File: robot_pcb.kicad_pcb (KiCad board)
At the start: 4 copper layers, 140 x 180 mm, 196 parts, among them J1 Raspberry_Pi_2_3, J10 Servo_TrayRelease, J14 Motor FR, J17 Programmer, J18 USB_C_Receptacle_PowerOnly_6P, J2 Power_Bypass, J23 Motor BR, J25 ConductClaw, J26 Motor BL, J27 TOF_Front, J28 OLED_Display, J29 Motor FL, J3 Lipo, J4 TOF_Right, J5 TOF_Back, J6 TOF_Claw, J7 UltraS_Side, J8 Servo_Grab, J9 Servo_Lift, Q2 Q_NMOS_GDS, SW1 SW_SPDT, SW2 SW_Push, U1 STM32F407VGTx, U10 DMG2305UX-7, U11 DMG2305UX-7, U2 BQ76920PW, U3 AP64501SP-13, U4 MAX25240AFFD/VY+, U5 DMG2305UX-7, U6 AP64501SP-13, U7 AP64501SP-13, U9 BNO086, Y1 25MHz, Y2 32.768kHz

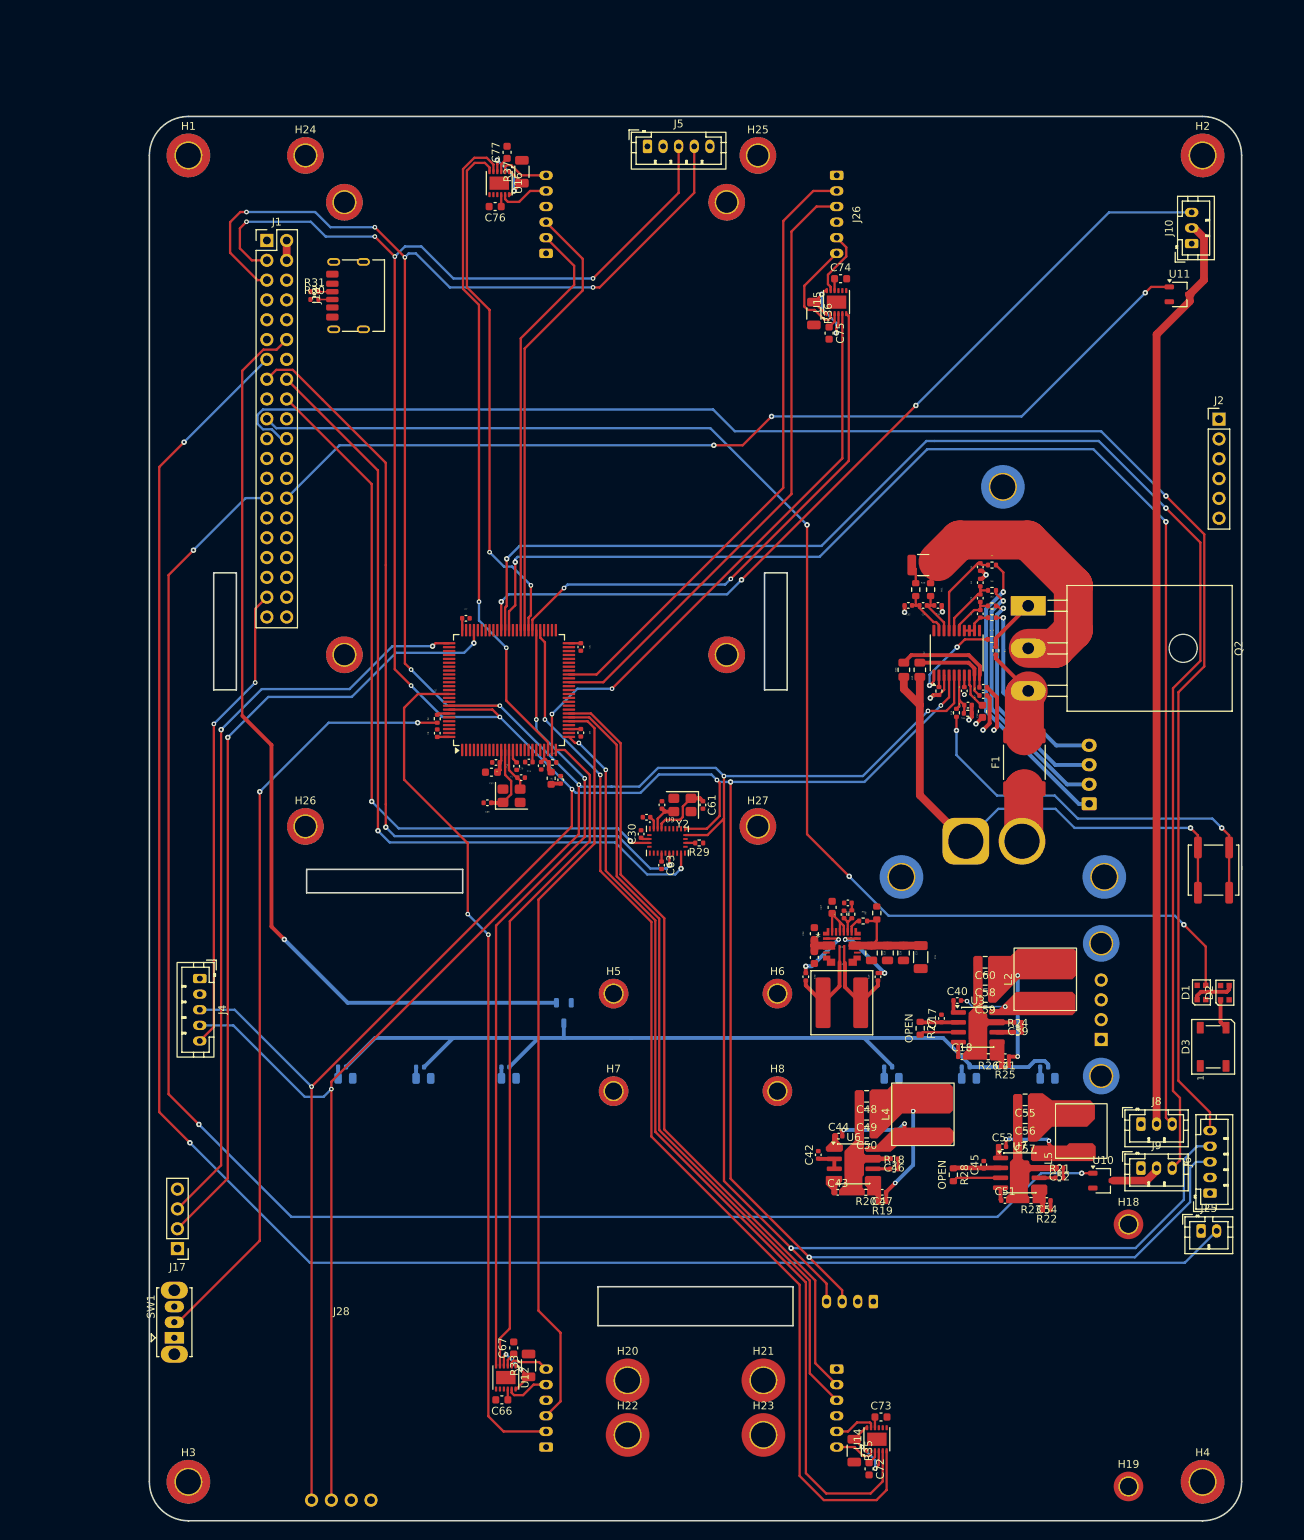
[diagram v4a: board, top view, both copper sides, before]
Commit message: Updated UserDrawings to add tof position and mounting holes
Had to reroute some traces, should be fine
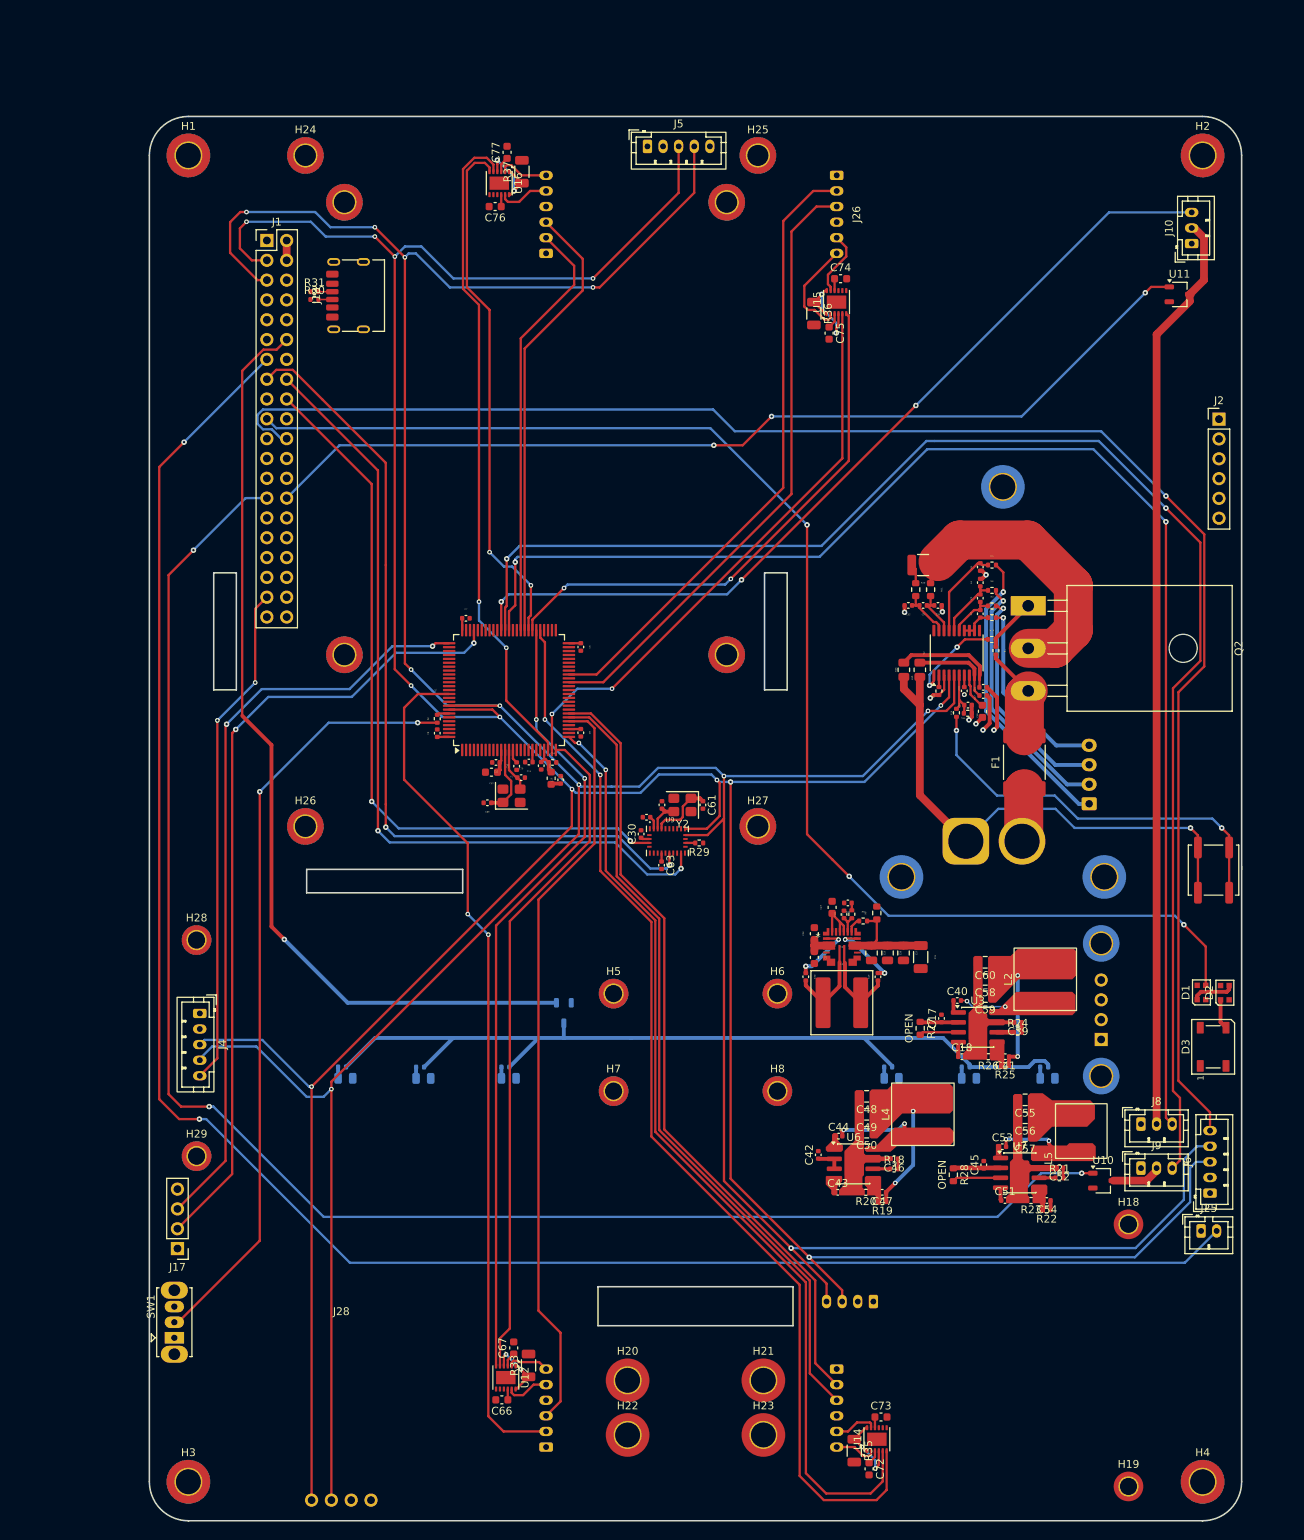
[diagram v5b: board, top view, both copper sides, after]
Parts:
- added H28: MountingHole, MountingHole:MountingHole_2.2mm_M2_DIN965_Pad_TopBottom, F.Cu at (40.6, 154.1)
- added H29: MountingHole, MountingHole:MountingHole_2.2mm_M2_DIN965_Pad_TopBottom, F.Cu at (40.6, 181.8)
- moved J4 4.47 mm to (41.0, 163.5)
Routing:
- net /GPIO26: track 60.4 -> 64.9 mm
- net /I2C_SDA: track 488.7 -> 487.3 mm
- net Net-(J1-GPIO27): track 247.4 -> 246.4 mm
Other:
- board text added: "ignore"

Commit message: cleaning up routing
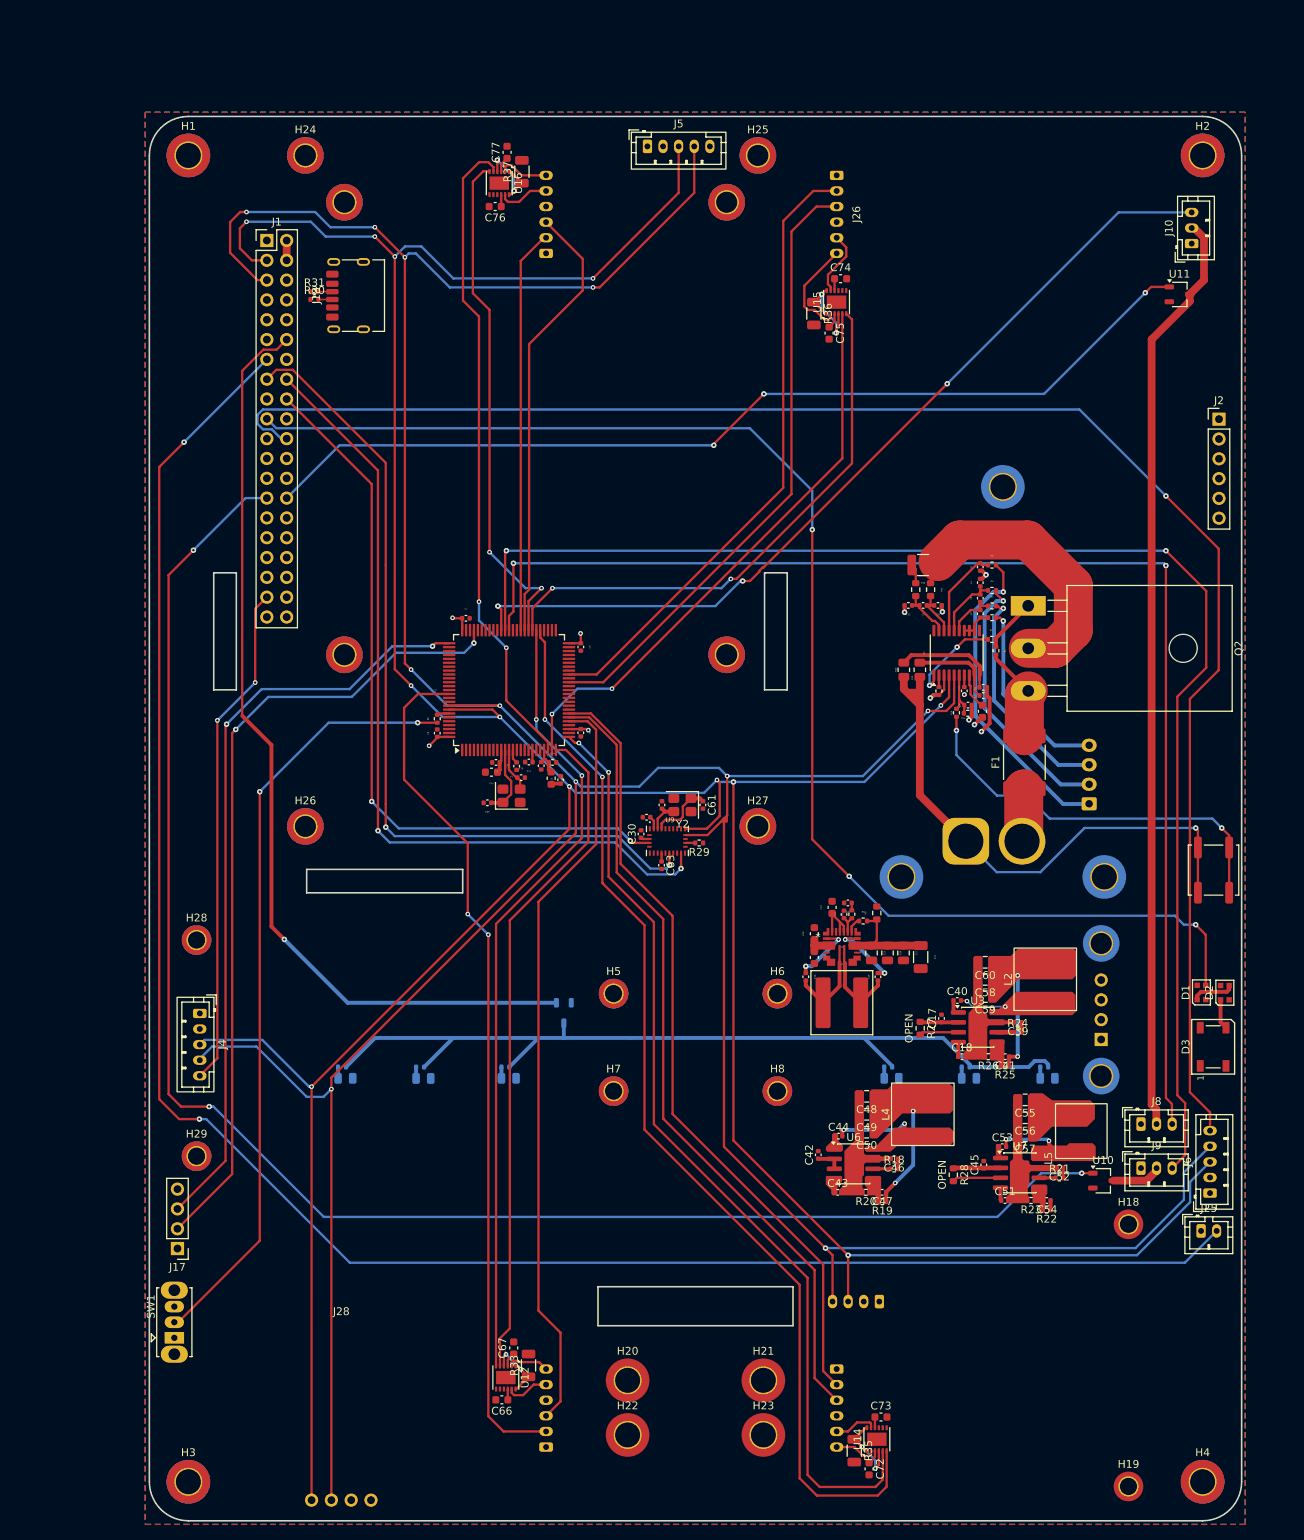
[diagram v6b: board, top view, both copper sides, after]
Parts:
- moved J27 0.76 mm to (128.1, 200.4)
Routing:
- net /TIM8_CH1: track 180.1 -> 164.5 mm
- net /TIM8_CH2: track 192.2 -> 178.8 mm
- net /I2C_SDA: track 487.3 -> 481.0 mm
- net +3.3V: track 14.8 -> 19.9 mm, vias 0 -> 4
- net /I2C_SCL: track 496.2 -> 491.6 mm
- net GND1: track 28.6 -> 24.0 mm, vias 9 -> 8
- net /GPIO10: track 176.6 -> 180.4 mm
- net Net-(J3-GND): track 38.2 -> 41.2 mm
- net /TIM4_CH2: track 54.6 -> 51.8 mm
- net +BATT: track 72.1 -> 73.8 mm
- net /PD10: track 69.3 -> 71.0 mm
- net /Battery/V1: track 32.8 -> 34.4 mm
- net /TIM5_CH1: track 84.7 -> 83.4 mm
- net /PD11: track 67.1 -> 65.9 mm
- net /TIM5_CH4: track 122.7 -> 122.0 mm
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- added copper zone on In2.Cu, net +3.3V
- added copper zone on B.Cu, net GND
- added copper zone on F.Cu, net GND
- added copper zone on In1.Cu, net GND

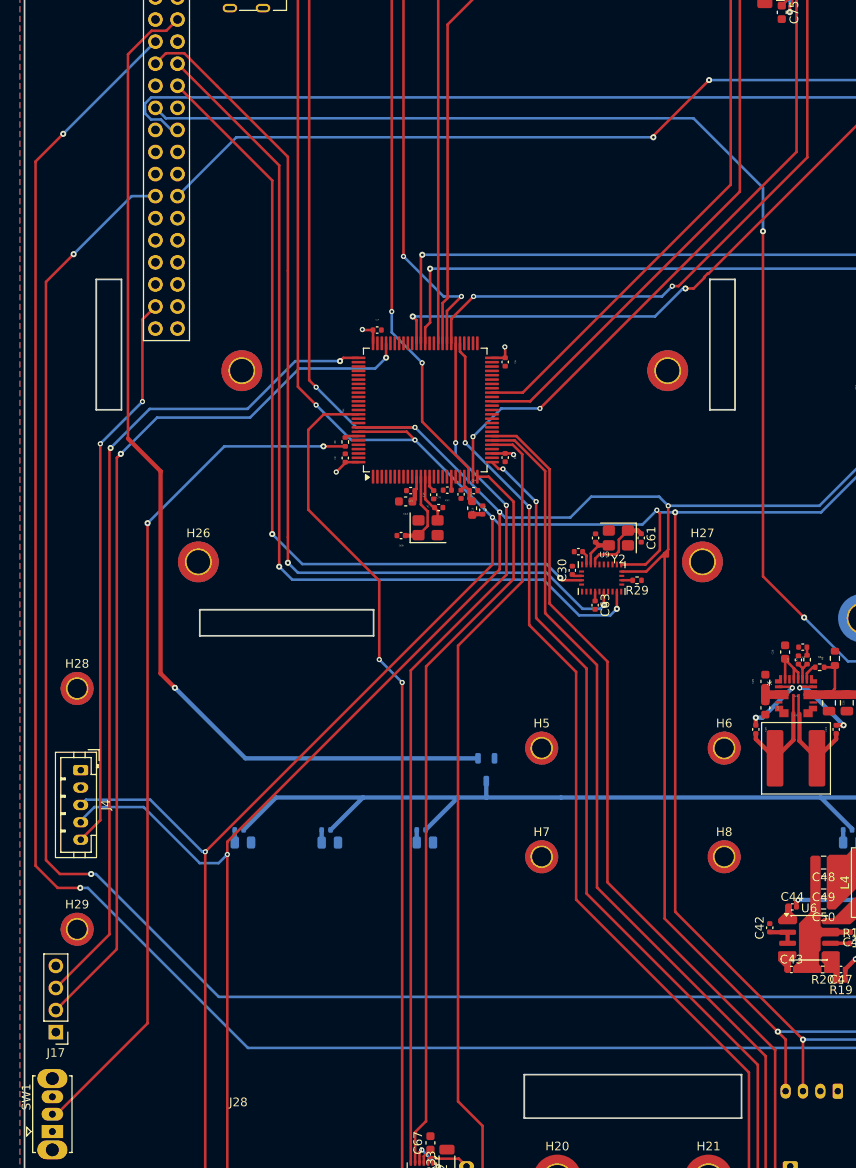
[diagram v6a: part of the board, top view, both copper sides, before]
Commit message: Added connector for PWM fan
Tachometer -> PI GPIO11
PWM -> PI PWM1
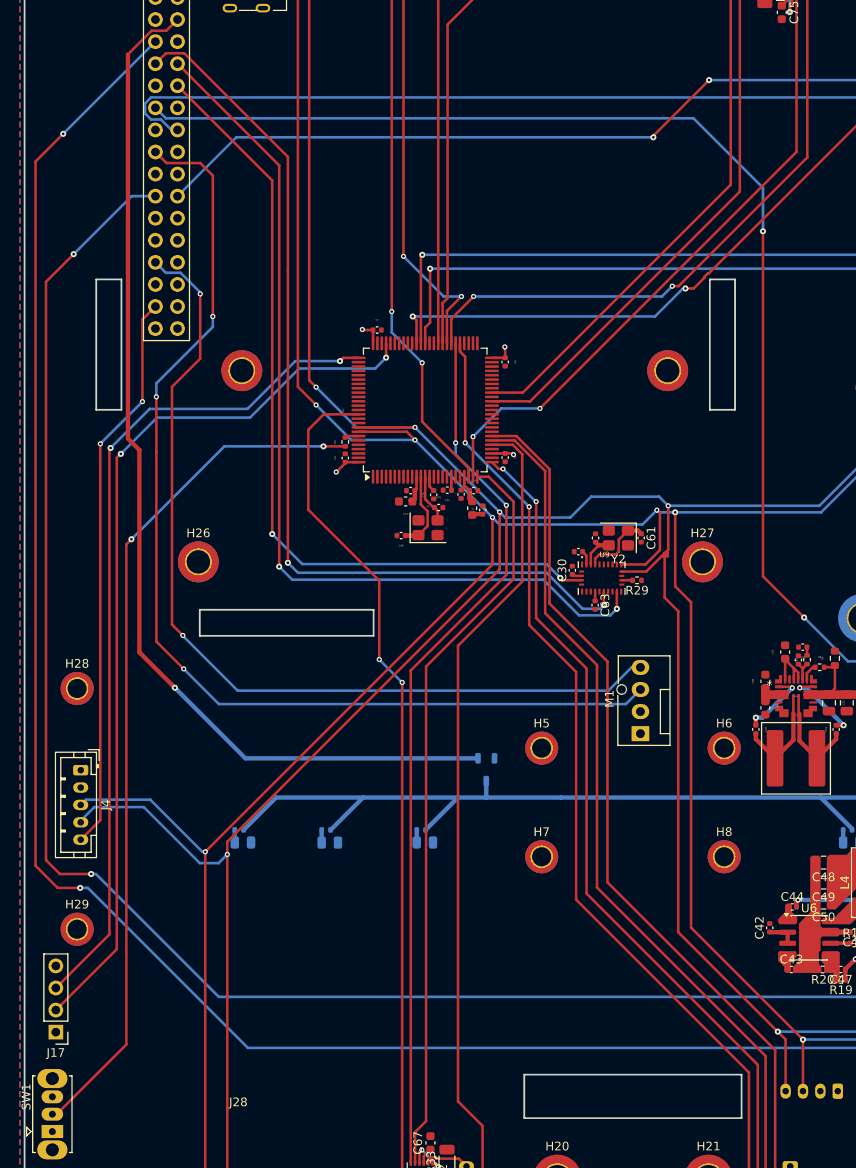
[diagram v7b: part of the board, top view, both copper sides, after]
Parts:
- added M1: Fan_Tacho_PWM, Connector:FanPinHeader_1x04_P2.54mm_Vertical, F.Cu at (105.4, 159.3)
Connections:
- J1 pad 23: unconnected-(J1-SCLK0/GPIO11-Pad23) -> /GPIO11
- J1 pad 33: unconnected-(J1-PWM1/GPIO13-Pad33) -> /PWM1
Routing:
- net /GPIO11: track 0.00 -> 123.4 mm, vias 0 -> 3
- net /PWM1: track 0.00 -> 104.3 mm, vias 0 -> 2

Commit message: 12v Routing
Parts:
- moved C75 1.49 mm to (121.7, 77.8)
- moved C77 1.04 mm to (80.4, 52.1)
- moved C67 0.99 mm to (81.2, 205.4)
- moved C74 0.87 mm to (124.0, 69.4)
- moved C72 0.44 mm to (126.8, 222.3)
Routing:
- net +12V: track 27.3 -> 102.4 mm, vias 0 -> 9
- net +3.3V: track 19.9 -> 26.7 mm, vias 4 -> 10
- net /TIM3_CH2: track 101.9 -> 102.6 mm
- added copper zone on In2.Cu, net +12V
